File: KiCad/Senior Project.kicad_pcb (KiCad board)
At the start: 4 copper layers, 59.2 x 89.2 mm, 68 parts, among them J1 USB_C_Receptacle_USB2.0_16P, J2 Screw_Terminal_01x02, J3 Screw_Terminal_01x06, Q2 IRLML0030, Q3 IRLML0030, Q4 IRLML0030, SW1 SW_Push, SW2 SW_Push, U1 ESP32-S3FH4R2, U2 TPS62162DSG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

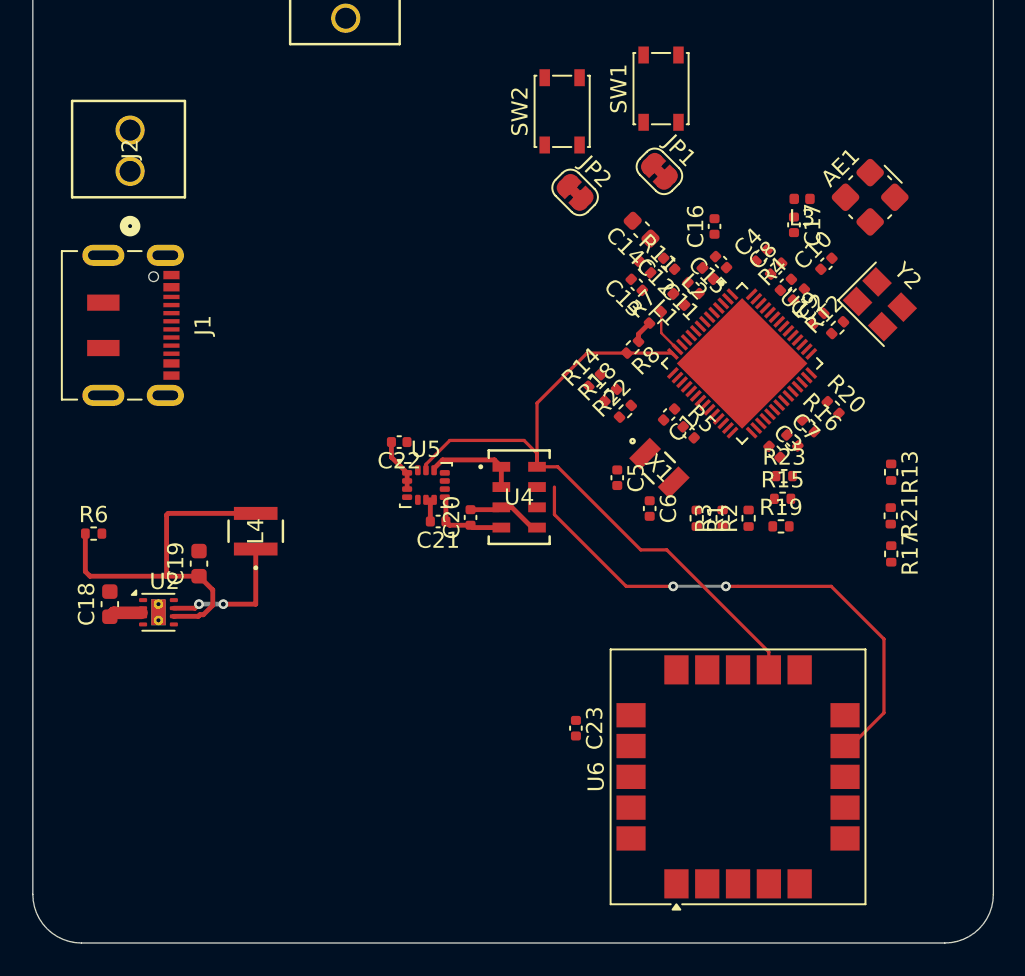
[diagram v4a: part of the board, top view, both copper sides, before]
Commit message: Routing, schematic fixes, and minor placement changes.
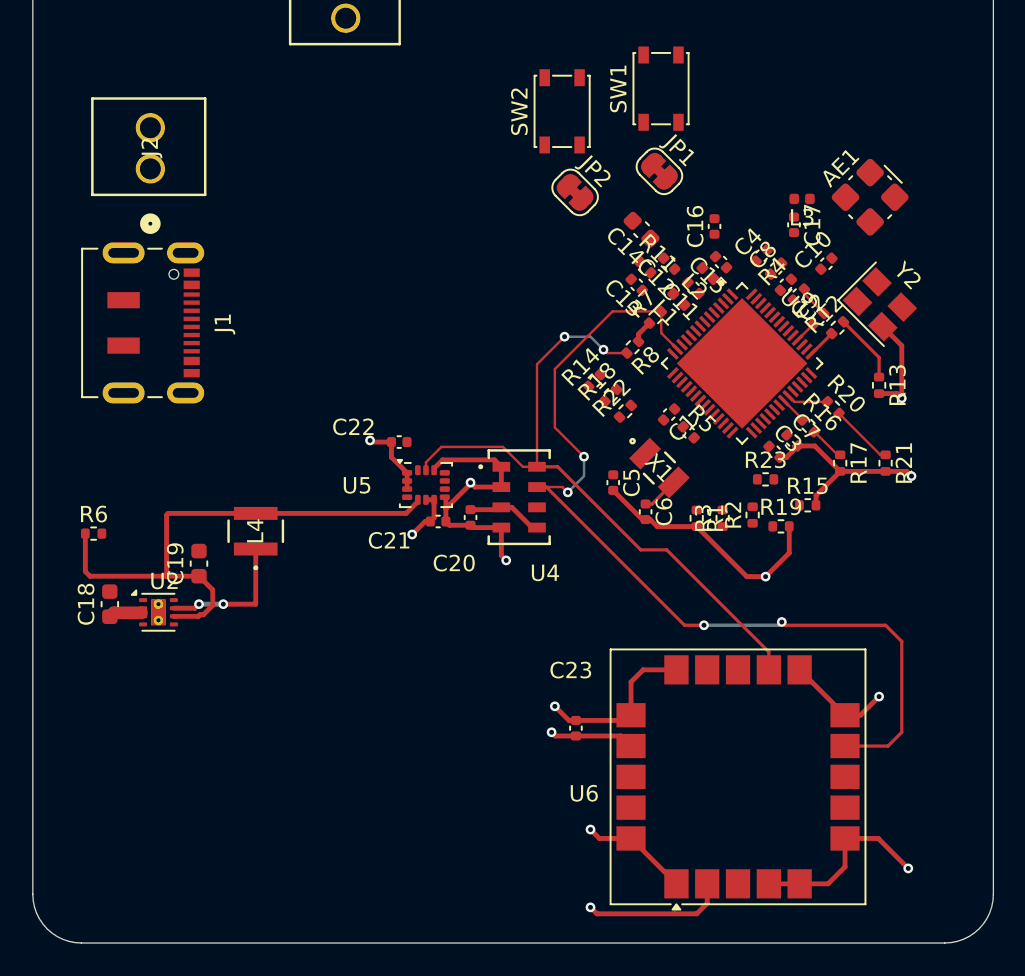
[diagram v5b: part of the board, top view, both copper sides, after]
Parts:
- moved R17 6.43 mm to (173.8, 109.4)
- moved R13 5.41 mm to (176.2, 104.6)
- moved R21 3.27 mm to (176.6, 109.4)
- moved R15 1.60 mm to (171.8, 112.0)
- moved J1 1.26 mm to (130.8, 100.8)
- moved J2 1.26 mm to (131.2, 91.2)
- moved R23 1.17 mm to (169.2, 110.4)
- moved C5 0.39 mm to (159.8, 110.6)
- moved C6 0.32 mm to (161.8, 112.4)
- moved R2 0.32 mm to (168.4, 112.6)
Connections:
- J1 pad A4: +BATT -> Net-(D1-K)
- J1 pad A9: +BATT -> Net-(D1-K)
- J1 pad B4: +BATT -> Net-(D1-K)
- J1 pad B9: +BATT -> Net-(D1-K)
- U1 pad 7: unconnected-(U1-GPIO2-Pad7) -> /GPS_Reset
- U6 pad 18: /Sensors/GPS_Reset -> /GPS_Reset
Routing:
- net GND: track 9.86 -> 83.4 mm, vias 0 -> 9
- net +3V3: track 35.9 -> 68.0 mm, vias 0 -> 4
- net /SDA: track 35.8 -> 57.6 mm, vias 2 -> 4
- net Net-(Q2-G): track 0.00 -> 4.32 mm
- net Net-(Q4-G): track 0.00 -> 3.94 mm
- net /Pyro GPIO 3: track 0.00 -> 2.56 mm
- net Net-(U1-XTAL_32K_N): track 0.00 -> 2.29 mm
- net Net-(Q3-G): track 0.00 -> 2.18 mm
- net /Pyro GPIO 1: track 0.00 -> 1.78 mm
- net /Pyro GPIO 2: track 0.00 -> 1.69 mm
- net /SCL: track 42.7 -> 41.4 mm, vias 0 -> 2

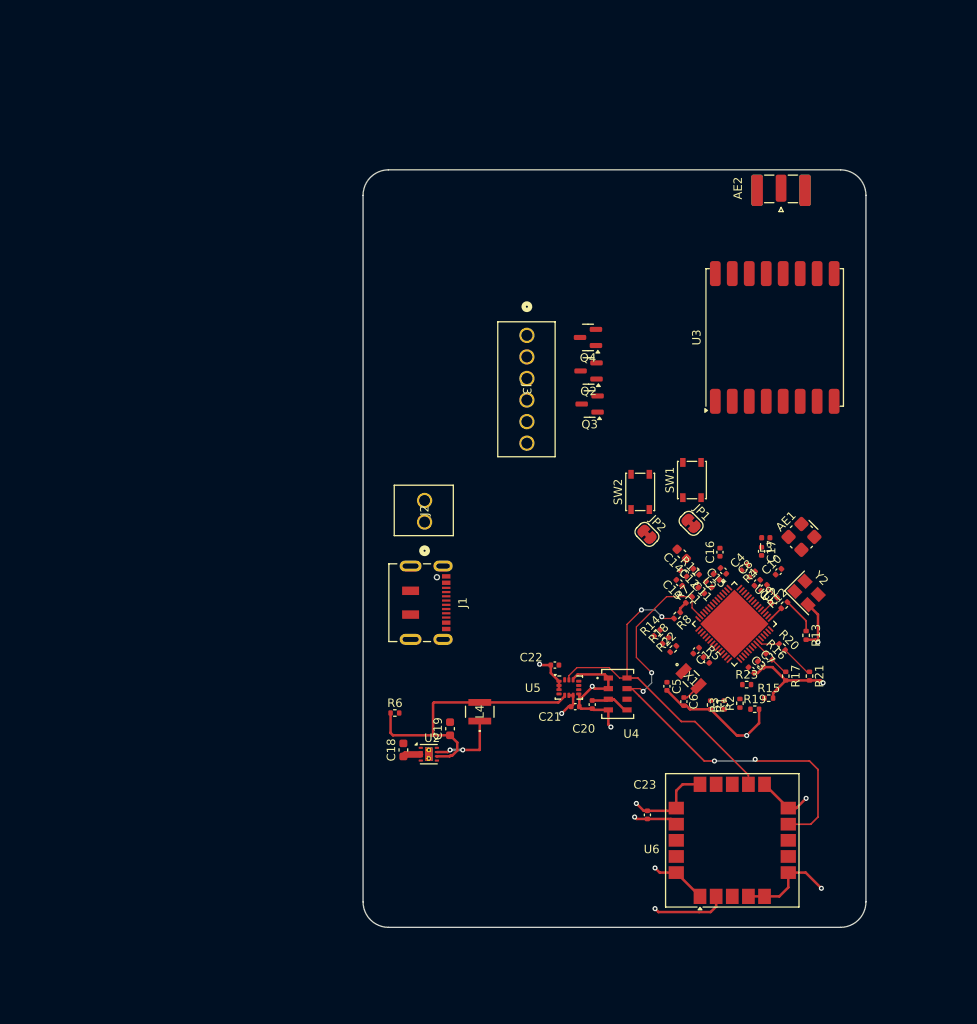
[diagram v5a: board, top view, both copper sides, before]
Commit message: Added ground support and 3.3 V via's
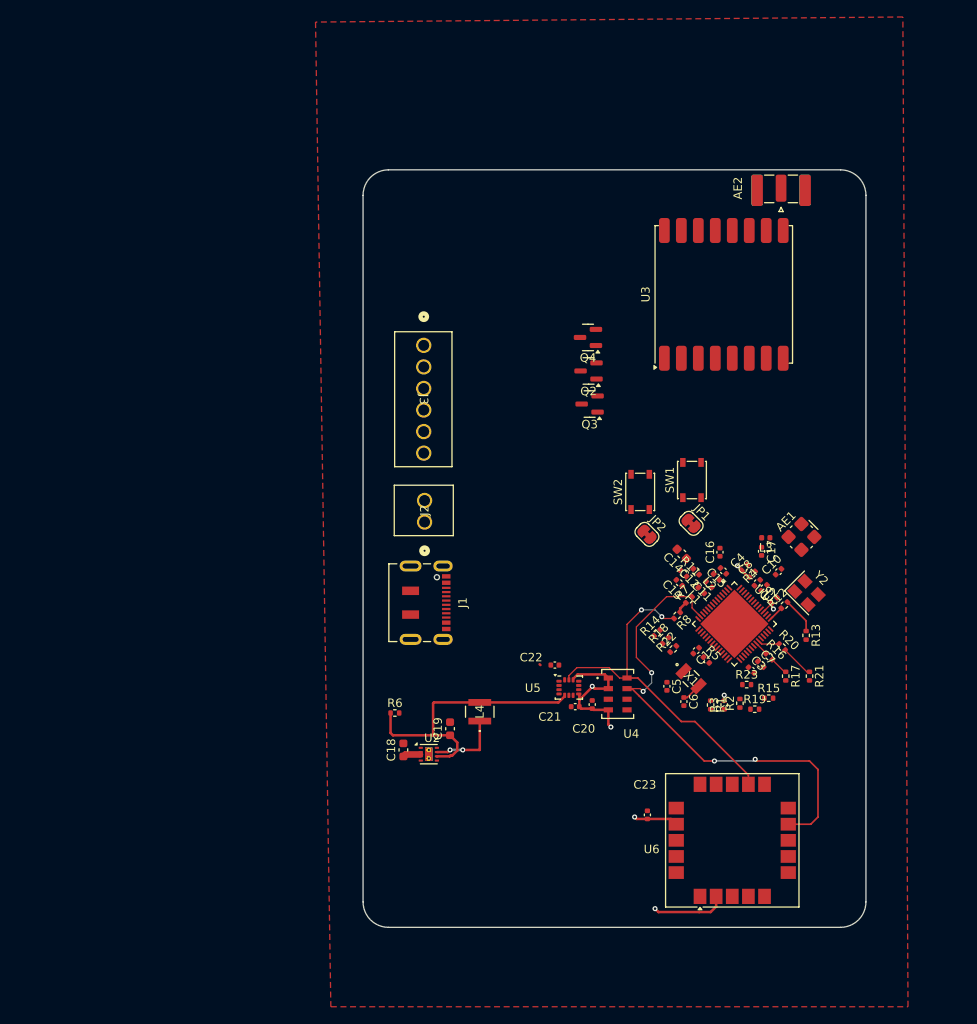
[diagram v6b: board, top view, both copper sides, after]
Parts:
- moved J3 12.2 mm to (131.2, 70.4)
- moved U3 7.86 mm to (166.5, 64.4)
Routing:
- net GND: track 83.4 -> 1.40 mm, vias 9 -> 0
- net +3V3: track 68.0 -> 71.4 mm, vias 4 -> 7
- added copper zone on F.Cu, net GND
- removed copper zone on In2.Cu, net GND

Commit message: a
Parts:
- moved R11 3.46 mm to (158.3, 97.5), turned to -135 degrees
- moved R14 1.28 mm to (157.7, 105.1)
- moved R18 1.28 mm to (158.7, 106.0)
- moved R22 1.28 mm to (159.6, 107.0)
- moved R5 0.82 mm to (163.9, 108.2)
- moved C5 0.38 mm to (159.4, 110.8)
- moved C1 0.32 mm to (163.5, 106.6)
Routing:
- net Net-(U1-XTAL_N): track 0.00 -> 12.0 mm, vias 0 -> 2
- net Net-(C10-Pad1): track 0.00 -> 3.08 mm
- net Net-(U1-VDD_SPI): track 0.00 -> 2.81 mm
- net /Sense 3: track 0.00 -> 0.53 mm
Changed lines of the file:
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@@
 	(footprint "Resistor_SMD:R_0402_1005Metric"
 		(layer "F.Cu")
-		(at 161.75 97.3 -45)
+		(at 158.3 97.55 -135)
 		(descr "Resistor SMD 0402 (1005 Metric), square (rectangular) end terminal, IPC_7351 nominal, (Body size source: IPC-SM-782 page 72, https://www.pcb-3d.com/wordpress/wp-content/uploads/ipc-sm-782a_amendment_1_and_2.pdf), generated with kicad-footprint-generator")
 		(tags "resistor")
 		(property "Reference" "R11"
-			(at 0 -1.17 135)
+			(at 0 -1.17 45)
 			(layer "F.SilkS")
 			(effects
@@
 		)
 		(property "Value" "100k"
-			(at 0 1.17 135)
+			(at 0 1.17 45)
 			(layer "F.Fab")
 			(effects
@@
 		)
 		(property "Datasheet" ""
-			(at 0 0 315)
+			(at 0 0 225)
 			(unlocked yes)
 			(layer "F.Fab")
@@
 		)
 		(property "Description" "Resistor, small symbol"
-			(at 0 0 315)
+			(at 0 0 225)
 			(unlocked yes)
 			(layer "F.Fab")
@@
 		)
 		(fp_line
-			(start -0.93 0.47)
-			(end -0.93 -0.47)
+			(start 0.93 0.47)
+			(end -0.93 0.47)
 			(stroke
 				(width 0.05)
@@
 		)
 		(fp_line
-			(start -0.93 -0.47)
-			(end 0.93 -0.47)
+			(start 0.93 -0.47)
+			(end 0.93 0.47)
 			(stroke
 				(width 0.05)
@@
 		)
 		(fp_line
-			(start 0.93 0.47)
-			(end -0.93 0.47)
+			(start -0.93 0.47)
+			(end -0.93 -0.47)
 			(stroke
 				(width 0.05)
@@
 		)
 		(fp_line
-			(start 0.93 -0.47)
-			(end 0.93 0.47)
+			(start -0.93 -0.47)
+			(end 0.93 -0.47)
 			(stroke
 				(width 0.05)
@@
 		)
 		(fp_line
-			(start -0.525 0.27)
-			(end -0.525 -0.27)
+			(start 0.525 0.27)
+			(end -0.525 0.27)
 			(stroke
 				(width 0.1)
@@
 		)
 		(fp_line
-			(start -0.525 -0.27)
-			(end 0.525 -0.27)
+			(start 0.525 -0.27)
+			(end 0.525 0.27)
 			(stroke
 				(width 0.1)
@@
 		)
 		(fp_line
-			(start 0.525 0.27)
-			(end -0.525 0.27)
+			(start -0.525 0.27)
+			(end -0.525 -0.27)
 			(stroke
 				(width 0.1)
@@
 		)
 		(fp_line
-			(start 0.525 -0.27)
-			(end 0.525 0.27)
+			(start -0.525 -0.27)
+			(end 0.525 -0.27)
 			(stroke
 				(width 0.1)
@@
 		)
 		(fp_text user "${REFERENCE}"
-			(at 0 0 135)
+			(at 0 0 45)
 			(layer "F.Fab")
 			(effects
@@
 		)
 		(pad "1" smd roundrect
-			(at -0.509999 0 315)
+			(at -0.509999 0 225)
 			(size 0.54 0.64)
 			(layers "F.Cu" "F.Mask" "F.Paste")
@@
 		)
 		(pad "2" smd roundrect
-			(at 0.509999 0 315)
+			(at 0.509999 0 225)
 			(size 0.54 0.64)
 			(layers "F.Cu" "F.Mask" "F.Paste")
@@
 	(footprint "Resistor_SMD:R_0402_1005Metric"
 		(layer "F.Cu")
-		(at 160.55 106.2 45)
+		(at 159.55 107 45)
 		(descr "Resistor SMD 0402 (1005 Metric), square (rectangular) end terminal, IPC_7351 nominal, (Body size source: IPC-SM-782 page 72, https://www.pcb-3d.com/wordpress/wp-content/uploads/ipc-sm-782a_amendment_1_and_2.pdf), generated with kicad-footprint-generator")
 		(tags "resistor")
@@
 	(footprint "Capacitor_SMD:C_0402_1005Metric"
 		(layer "F.Cu")
-		(at 159.8 110.6 -90)
+		(at 159.45 110.75 -90)
 		(descr "Capacitor SMD 0402 (1005 Metric), square (rectangular) end terminal, IPC_7351 nominal, (Body size source: IPC-SM-782 page 76, https://www.pcb-3d.com/wordpress/wp-content/uploads/ipc-sm-782a_amendment_1_and_2.pdf), generated with kicad-footprint-generator")
 		(tags "capacitor")
@@
 	(footprint "Capacitor_SMD:C_0402_1005Metric"
 		(layer "F.Cu")
-		(at 163.25 106.4 -135)
+		(at 163.5 106.6 -135)
 		(descr "Capacitor SMD 0402 (1005 Metric), square (rectangular) end terminal, IPC_7351 nominal, (Body size source: IPC-SM-782 page 76, https://www.pcb-3d.com/wordpress/wp-content/uploads/ipc-sm-782a_amendment_1_and_2.pdf), generated with kicad-footprint-generator")
 		(tags "capacitor")
@@
 	(footprint "Capacitor_SMD:C_0402_1005Metric"
 		(layer "F.Cu")
-		(at 164.45 107.5 -45)
+		(at 163.95 108.15 -45)
 		(descr "Capacitor SMD 0402 (1005 Metric), square (rectangular) end terminal, IPC_7351 nominal, (Body size source: IPC-SM-782 page 76, https://www.pcb-3d.com/wordpress/wp-content/uploads/ipc-sm-782a_amendment_1_and_2.pdf), generated with kicad-footprint-generator")
 		(tags "capacitor")
@@
 	(footprint "Resistor_SMD:R_0402_1005Metric"
 		(layer "F.Cu")
-		(at 158.65 104.3 45)
+		(at 157.65 105.1 45)
 		(descr "Resistor SMD 0402 (1005 Metric), square (rectangular) end terminal, IPC_7351 nominal, (Body size source: IPC-SM-782 page 72, https://www.pcb-3d.com/wordpress/wp-content/uploads/ipc-sm-782a_amendment_1_and_2.pdf), generated with kicad-footprint-generator")
 		(tags "resistor")
@@
 	(footprint "Resistor_SMD:R_0402_1005Metric"
 		(layer "F.Cu")
-		(at 159.65 105.2 45)
+		(at 158.65 106 45)
 		(descr "Resistor SMD 0402 (1005 Metric), square (rectangular) end terminal, IPC_7351 nominal, (Body size source: IPC-SM-782 page 72, https://www.pcb-3d.com/wordpress/wp-content/uploads/ipc-sm-782a_amendment_1_and_2.pdf), generated with kicad-footprint-generator")
 		(tags "resistor")
@@
 	)
 	(segment
-		(start 144.9 108.1)
-		(end 144.8 108)
-		(width 0.300387)
-		(layer "F.Cu")
-		(net 2)
-	)
-	(segment
 		(start 154.796712 113.375)
 		(end 155.1 113.375)
@@
 	)
 	(segment
+		(start 178.555635 98.85)
+		(end 177.628858 99.776777)
+		(width 0.2)
+		(layer "F.Cu")
+		(net 4)
+	)
+	(segment
+		(start 171.471178 99.9)
+		(end 171.75 99.9)
+		(width 0.2)
+		(layer "F.Cu")
+		(net 4)
+	)
+	(segment
+		(start 170.910589 99.339411)
+		(end 171.471178 99.9)
+		(width 0.2)
+		(layer "F.Cu")
+		(net 4)
+	)
+	(segment
+		(start 171.75 99.9)
+		(end 172.961324 98.688676)
+		(width 0.2)
+		(layer "F.Cu")
+		(net 4)
+	)
+	(segment
+		(start 172.961324 98.688676)
+		(end 173.011324 98.688676)
+		(width 0.2)
+		(layer "F.Cu")
+		(net 4)
+	)
+	(segment
+		(start 178.7 98.85)
+		(end 178.555635 98.85)
+		(width 0.2)
+		(layer "F.Cu")
+		(net 4)
+	)
+	(via
+		(at 173.011324 98.688676)
+		(size 0.6)
+		(drill 0.3)
+		(layers "F.Cu" "B.Cu")
+		(net 4)
+	)
+	(via
+		(at 178.7 98.85)
+		(size 0.6)
+		(drill 0.3)
+		(layers "F.Cu" "B.Cu")
+		(net 4)
+	)
+	(segment
+		(start 178.7 98.65)
+		(end 178.7 98.85)
+		(width 0.2)
+		(layer "B.Cu")
+		(net 4)
+	)
+	(segment
+		(start 175.1 96.65)
+		(end 176.95 96.65)
+		(width 0.2)
+		(layer "B.Cu")
+		(net 4)
+	)
+	(segment
+		(start 173.061324 98.688676)
+		(end 175.05 96.7)
+		(width 0.2)
+		(layer "B.Cu")
+		(net 4)
+	)
+	(segment
+		(start 173.011324 98.688676)
+		(end 173.061324 98.688676)
+		(width 0.2)
+		(layer "B.Cu")
+		(net 4)
+	)
+	(segment
+		(start 175.05 96.7)
+		(end 175.1 96.65)
+		(width 0.2)
+		(layer "B.Cu")
+		(net 4)
+	)
+	(segment
+		(start 178.7 98.4)
+		(end 178.7 98.65)
+		(width 0.2)
+		(layer "B.Cu")
+		(net 4)
+	)
+	(segment
+		(start 176.95 96.65)
+		(end 178.7 98.4)
+		(width 0.2)
+		(layer "B.Cu")
+		(net 4)
+	)
+	(segment
+		(start 169.810589 108.360589)
+		(end 170.510589 107.660589)
+		(width 0.2)
+		(layer "F.Cu")
+		(net 5)
+	)
+	(segment
+		(start 169.410589 108.360589)
+		(end 169.810589 108.360589)
+		(width 0.2)
+		(layer "F.Cu")
+		(net 5)
+	)
+	(segment
+		(start 169.168077 108.360589)
+		(end 168.332655 107.525167)
+		(width 0.2)
+		(layer "F.Cu")
+		(net 5)
+	)
+	(segment
+		(start 169.410589 108.360589)
+		(end 169.168077 108.360589)
+		(width 0.2)
+		(layer "F.Cu")
+		(net 5)
+	)
+	(segment
 		(start 161.8 111.92)
 		(end 162.197766 111.92)
@@
 	)
 	(segment
+		(start 172.610589 97.439411)
+		(end 174.594401 99.423223)
+		(width 0.2)
+		(layer "F.Cu")
+		(net 8)
+	)
+	(segment
+		(start 174.594401 99.423223)
+		(end 174.871142 99.423223)
+		(width 0.2)
+		(layer "F.Cu")
+		(net 8)
+	)
+	(segment
 		(start 128.991719 118.631831)
 		(end 130.708281 118.631831)
@@
 	)
 	(segment
+		(start 165.725555 106.103176)
+		(end 165.425788 106.402943)
+		(width 0.15)
+		(layer "F.Cu")
+		(net 65)
+	)
+	(segment
+		(start 165.745352 106.103176)
+		(end 165.725555 106.103176)
+		(width 0.15)
+		(layer "F.Cu")
+		(net 65)
+	)
+	(segment
+		(start 168.69 110.4)
+		(end 168.69 110.39)
+		(width 0.2)
+		(layer "F.Cu")
+		(net 67)
+	)
+	(segment
+		(start 165.660271 106.753943)
+		(end 166.028195 106.386019)
+		(width 0.15)
+		(layer "F.Cu")
+		(net 67)
+	)
+	(segment
 		(start 173.281176 101.404624)
 		(end 173.281176 101.411336)
@@
 		(layer "In1.Cu")
 		(hatch edge 0.5)
-		(connect_pads
+		(connect_pads yes
 			(clearance 0.25)
 		)

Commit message: Added Diodes and did some routing
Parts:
- added D1: D, VS_10BQ015HM3_5BT:CR_SMBDO-214AA_VIS, F.Cu at (140.1, 101.8)
- added D2: D, VS_10BQ015HM3_5BT:CR_SMBDO-214AA_VIS, F.Cu at (131.5, 109.5)
- C10, C2: value TBD -> 15p
- C5: value TBD -> 20pf
- C6: value TBD -> 20p
- R4: value TBD -> 24 nF
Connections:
- C18 pad 1: +BATT -> +VDC
- U2 pad 2: +BATT -> +VDC
- U2 pad 3: +BATT -> +VDC
- U2 pad 8: /PowerReg/PG -> GND
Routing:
- net +VDC: track 0.00 -> 2.06 mm
- net +BATT: track 2.06 -> 0.00 mm
